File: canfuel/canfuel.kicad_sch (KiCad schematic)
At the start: 0 parts

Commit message: Draw canfuel schematic
One A3 sheet, 22 components, 31 nets. A4 was tried first and every block
collided with its neighbour - the part count is low but the label count
is not.

All four failure modes from section 3 of the implementation plan are on
the sheet and repeated as numbered notes on it, so they survive even if
someone opens the schematic without the plan: MCP2562 VIO to +5V and STBY
to SGND, R5 120R not fitted, 33 pF crystal loading, both Micro-Fit headers
in parallel, and 10 uF on VDDCORE/VCAP with pin 6 never tied to +5V.

Labels are global rather than local. On one sheet either works, but a
local label reaches the netlist as /CANH while the net classes in plan
section 5.3 are written CANH, and a netclass pattern matching nothing is
a bad way to discover that CAN got routed at the default track width.

U1 uses the SSOP-28 symbol with a PDIP-28 socket footprint - KiCad ships
no SPDIP variant for this part and all three 28-pin packages share one
pinout, verified pin by pin against DS39977C page 6.

ERC is clean at --severity-all with nothing silenced; three PWR_FLAGs
were needed because +5V and SGND come from a connector and VCAP from the
regulator inside U1. Separately, the exported netlist was compared
connection by connection against the plan's tables - 97 connections, no
pin unaccounted for. ERC cannot tell RB2 from RB3; that comparison can.

Co-Authored-By: Claude Opus 5 <noreply@anthropic.com>
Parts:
- added C1, C2: 33p, Capacitor_THT:C_Disc_D5.0mm_W2.5mm_P5.00mm, symbol Device:C
- added C3, C4, C5: 100n, Capacitor_THT:C_Disc_D5.0mm_W2.5mm_P5.00mm, symbol Device:C
- added C6: 10u, Capacitor_THT:CP_Radial_D5.0mm_P2.50mm, symbol Device:C_Polarized
- added C7: 10u, Capacitor_THT:C_Disc_D7.5mm_W5.0mm_P5.00mm, symbol Device:C
- added D1: green, LED_THT:LED_D3.0mm, symbol Device:LED
- added D2: yellow, LED_THT:LED_D3.0mm, symbol Device:LED
- added J1, J2: Micro-Fit 43045-0400, Connector_Molex:Molex_Micro-Fit_3.0_43045-0400_2x02_P3.00mm_Horizontal, symbol Connector_Generic:Conn_02x02_Odd_Even
- added J3: ICSP, Connector_PinHeader_2.54mm:PinHeader_1x05_P2.54mm_Vertical, symbol Connector_Generic:Conn_01x05
- added J4: ESCAPE, Connector_PinHeader_2.54mm:PinHeader_2x08_P2.54mm_Vertical, symbol Connector_Generic:Conn_02x08_Odd_Even
- added JP1: DBG, Connector_PinHeader_2.54mm:PinHeader_1x02_P2.54mm_Vertical, symbol Connector_Generic:Conn_01x02
- added R1, R2: 10k, Resistor_THT:R_Axial_DIN0207_L6.3mm_D2.5mm_P10.16mm_Horizontal, symbol Device:R
- added R3, R4: 1k, Resistor_THT:R_Axial_DIN0207_L6.3mm_D2.5mm_P10.16mm_Horizontal, symbol Device:R
- added R5: 120R, Resistor_THT:R_Axial_DIN0207_L6.3mm_D2.5mm_P10.16mm_Horizontal, symbol Device:R
- added U1: PIC18F25K80, Package_DIP:DIP-28_W7.62mm_Socket, symbol MCU_Microchip_PIC18:PIC18F25K80_ISS
- added U2: MCP2562-E/P, Package_DIP:DIP-8_W7.62mm_Socket, symbol Interface_CAN_LIN:MCP2562-E-P
- added Y1: 16MHz, Crystal:Crystal_HC49-U_Vertical, symbol Device:Crystal
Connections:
- new net +5V: C3.1, C4.1, C5.1, C6.1, J1.1 (Pin_1), J2.1 (Pin_1), J3.2 (Pin_2), J4.14 (Pin_14), JP1.1 (Pin_1), R1.1, U1.20 (Vdd), U2.3 (VDD), U2.5 (Vio)
- new net CANH: J1.3 (Pin_3), J2.3 (Pin_3), R5.1, U2.7 (CANH)
- new net CANL: J1.4 (Pin_4), J2.4 (Pin_4), R5.2, U2.6 (CANL)
- new net CANRX2: J4.4 (Pin_4), U1.18 (CANRX/RX1/CCP4/RC7)
- new net CANTX2: J4.2 (Pin_2), U1.17 (CANTX/TX1/CCP3/RC6)
- new net CAN_RX: U1.24 (CANRX/INT3/RB3), U2.4 (RXD)
- new net CAN_TX: U1.23 (CANTX/INT2/RB2), U2.1 (TXD)
- new net DBG_EN: JP1.2 (Pin_2), R2.1, U1.2 (RA0/AN0)
- new net ESC_RA3: J4.1 (Pin_1), U1.5 (RA3/Vref+/AN3)
- new net ESC_RA5: J4.3 (Pin_3), U1.7 (RA5/AN4)
- new net ESC_RB0: J4.6 (Pin_6), U1.21 (AN10/INT0/RB0)
- new net ESC_RB1: J4.8 (Pin_8), U1.22 (AN8/INT1/RB1)
- new net ESC_RB4: J4.10 (Pin_10), U1.25 (AN9/ECCP1/RB4)
- new net ESC_RB5: J4.12 (Pin_12), U1.26 (CCP5/RB5)
- new net ESC_RC0: J4.5 (Pin_5), U1.11 (SOSCO/RC0)
- new net ESC_RC1: J4.7 (Pin_7), U1.12 (SOSCI/RC1)
- new net ESC_RC2: J4.9 (Pin_9), U1.13 (CCP2/RC2)
- new net ESC_RC3: J4.11 (Pin_11), U1.14 (SCL/SCK/RC3)
- new net ESC_RC4: J4.13 (Pin_13), U1.15 (SDA/SDI/RC4)
- new net ESC_RC5: J4.15 (Pin_15), U1.16 (SDO/RC5)
- new net LED_CAN: R4.1, U1.4 (RA2/Vref-/AN2)
- new net LED_CAN_A: D2.2 (A), R4.2
- new net LED_PWR: R3.1, U1.3 (RA1/AN1)
- new net LED_PWR_A: D1.2 (A), R3.2
- new net OSC1: C1.1, U1.9 (OSC1/CLKIN), Y1.1
- new net OSC2: C2.1, U1.10 (OSC2/CLKOUT), Y1.2
- new net PGC: J3.5 (Pin_5), U1.27 (PGC/TX2/RB6)
- new net PGD: J3.4 (Pin_4), U1.28 (PGD/RX2/RB7)
- new net SGND: C1.2, C2.2, C3.2, C4.2, C5.2, C6.2, C7.2, D1.1 (K), D2.1 (K), J1.2 (Pin_2), J2.2 (Pin_2), J3.3 (Pin_3), J4.16 (Pin_16), R2.2, U1.19 (Vss), U1.8 (Vss), U2.2 (VSS), U2.8 (STBY)
- new net VCAP: C7.1, U1.6 (Vcap)
- new net ~{MCLR}: J3.1 (Pin_1), R1.2, U1.1 (~{MCLR}/RE3)
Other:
- note added: "5 J1 and J2 are wired in parallel on the same four nets, so the cables are interchangeable and the board passes CAN through even with U1 out of its socket. Micro-Fit pin 1 = +5V, 2 = SGND, 3 = CANH, 4 = CANL, fixed by the harness. 6 Decoupling: C3 at U1 pin 20, C4 at U2 pin 3, C5 at U2 pin 5. 7 No pull-ups, series diodes or capacitors on PGC/PGD - they interfere with the programmer. DS39977C 2.5.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"
- note added: "NOTES 1 U2 VIO (pin 5) to +5V and STBY (pin 8) to SGND are both mandatory. Left off, the transceiver sits in standby and sends nothing while every other measurement looks correct. 2 C7 is 10 uF low-ESR on VDDCORE/VCAP (U1 pin 6) and is not optional - the core regulator is unstable without it. Pin 6 is not a port pin and must NEVER go to +5V. Keep the PCB track to C7 under 6 mm. DS39977C 2.4 and t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"
- company: (none) -> PoJD
- title: (none) -> canfuel - CAN fuel consumption converter

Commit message: Re-check the schematic against the manufacturer datasheets
Adopts a sourcing rule for this repository: every hardware fact comes from the
manufacturer's datasheet for the exact part, cited by document and section, and
an open question is asked rather than filled in with a plausible number. The
rule is in CLAUDE.md; implementation-plan.md section 10 lists what has actually
been read out of each datasheet, so a checked number can be told from an
inherited one.

Applying it to the drawn sheet found three things.

The LEDs were on RA1/RA2, which are inside PORTA<5:0>. DS39977C page 541 caps
those pins at 2 mA sourced or sunk, against 25 mA for PORTB and PORTC; 1 kohm
from a 5 V rail draws about 2.2 mA once VOH is taken as VDD-0.7. They move to
RC0 (pin 11) and RC1 (pin 12) and RA1/RA2 take the escape-header slots RC0/RC1
vacate, so J4 stays 2x8 and the board is unchanged. The DC characteristics
table specifies PORTA at IOH = -3 mA and so reads like permission; absolute
maximums win. PoJD/can-pcb was not a precedent for the 1 kohm - its status LED
is on RC1, and the port was the part that mattered.

MCLR had only the 10k pull-up, with a note reading "no capacitor on this pin".
That was section 2.5, which is about PGC and PGD, applied to MCLR. Section 2.3
asks for the capacitor and hands it a jumper in the same paragraph, so the full
Figure 2-2 network goes in: R6 470R in series into pin 1, C8 100n to SGND
behind JP2. JP2 comes off before programming.

The crystal was documented as CL = 32 pF. That figure is in no datasheet and
does not survive the arithmetic - 32 pF would want about 56 pF of loading. The
supplied crystal datasheet gives 20 pF standard, and C = 2*(20-5) = 30 pF puts
the fitted 33 pF exactly where it should be. The value was right for the wrong
reason. No series resistor on OSC2: the drive level argues for one, the
datasheet only says "may be required", and it cannot be settled without
measuring a built board.

Also recorded: STBY floats high through an in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
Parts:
- added C8: 100n, Capacitor_THT:C_Disc_D5.0mm_W2.5mm_P5.00mm, symbol Device:C
- added JP2: MCLR, Connector_PinHeader_2.54mm:PinHeader_1x02_P2.54mm_Vertical, symbol Connector_Generic:Conn_01x02
- added R6: 470R, Resistor_THT:R_Axial_DIN0207_L6.3mm_D2.5mm_P10.16mm_Horizontal, symbol Device:R
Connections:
- net ESC_RA3: now also J4.5 (Pin_5); no longer J4.1 (Pin_1)
- net ESC_RA5: now also J4.7 (Pin_7); no longer J4.3 (Pin_3)
- net LED_CAN: now also U1.12 (SOSCI/RC1); no longer U1.4 (RA2/Vref-/AN2)
- net LED_PWR: now also U1.11 (SOSCO/RC0); no longer U1.3 (RA1/AN1)
- net SGND: now also C8.2
- net ~{MCLR}: now also R6.2; no longer R1.2
- removed net ESC_RC0: J4.5 (Pin_5), U1.11 (SOSCO/RC0)
- removed net ESC_RC1: J4.7 (Pin_7), U1.12 (SOSCI/RC1)
- new net ESC_RA1: J4.1 (Pin_1), U1.3 (RA1/AN1)
- new net ESC_RA2: J4.3 (Pin_3), U1.4 (RA2/Vref-/AN2)
- new net MCLR_C: C8.1, JP2.2 (Pin_2)
- new net MCLR_RC: JP2.1 (Pin_1), R1.2, R6.1
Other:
- note added: "10 D1 and D2 sit on RC0 and RC1, not on port A. DS39977C page 541 allows PORTA<5:0> only 2 mA sourced or sunk, against 25 mA on PORTB and PORTC. RA1 and RA2 went to J4 instead. 11 MCLR carries the full network of DS39977C figure 2-2: R1 10k to +5V, R6 470R in series into pin 1, C8 100n to SGND behind JP2. Pull the JP2 jumper before programming - note 7."

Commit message: Pin C6 and C7 to the parts that will actually be fitted
Both capacitors carried a footprint that no purchasable part matched, which
would have surfaced during layout at the earliest and during assembly at the
worst.

C6 was drawn on a 2.50 mm radial pattern. The electrolytic bought for it is a
5 x 11 mm RM2 part, so the footprint becomes CP_Radial_D5.0mm_P2.00mm.

C7 was drawn as a 5 mm ceramic disc, and no such 10 uF part exists to buy -
GME's through-hole ceramic range stops at 1 uF. It becomes a Murata
GRM32DR71C106KA01L in 1210, which is one of the four parts DS39977C Table 2-1
names for this pin, so its suitability needs no equivalence argument: ESR in
milliohms against a 5 ohm limit, and enough DC-bias headroom in a 1210 X7R at
3.3 V to stay clear of the 4.7 uF minimum in Table 31-4.

A dipped tantalum was the obvious way to keep the board entirely through-hole
and was rejected on the evidence. The CA42 datasheet gives DF = 6 % at 100 Hz
across the 10-68 uF range, which is 9.6 ohm there, and specifies no
high-frequency ESR at all. The true figure is probably 2-3 ohm and PoJD/can-pcb
has run one for years, but that is experience rather than specification, and
this is the part whose failure mode section 3.5 already describes as
intermittent and unpleasant to debug. Recorded in the plan so the option is not
reopened from memory. A tantalum would also have needed C_Polarized and a
polarity mark; can-pcb drew its as a non-polarised C-EU, which was safe only
because the builder knew which way round it went.

C7 is now the only SMD part on the board. That buys something back: at 1210 it
goes on B.Cu directly under pin 6, which turns the 6 mm track limit of section
2.4 - the one numeric placement constraint on this board - into roughly zero.

Also relaxes the buying rule for resistors and LEDs, which was inherited
without a reason. Neither has an electrolyte or a hidden parameter, so neither
ages in a drawer; the rule was only ever about the electrolytic and about a
c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
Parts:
- C6: footprint Capacitor_THT:CP_Radial_D5.0mm_P2.50mm -> Capacitor_THT:CP_Radial_D5.0mm_P2.00mm
- C7: footprint Capacitor_THT:C_Disc_D7.5mm_W5.0mm_P5.00mm -> Capacitor_SMD:C_1210_3225Metric_Pad1.33x2.70mm_HandSolder
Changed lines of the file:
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@@
 		(property
 			"Footprint"
-			"Capacitor_THT:C_Disc_D7.5mm_W5.0mm_P5.00mm"
+			"Capacitor_SMD:C_1210_3225Metric_Pad1.33x2.70mm_HandSolder"
 			(at 99.06 76.2 0)
 			(show_name no)
@@
 		(property
 			"Footprint"
-			"Capacitor_THT:CP_Radial_D5.0mm_P2.50mm"
+			"Capacitor_THT:CP_Radial_D5.0mm_P2.00mm"
 			(at 91.44 215.9 0)
 			(show_name no)

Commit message: Place canfuel PCB parts
Net classes, all 25 footprints, and a silkscreen that can be read. Nothing is
routed yet; DRC is clean and the 70 unconnected items are the ratsnest.

The MCLR network cannot meet DS39977C 2.3 in full. Four parts totalling 71 mm2
of courtyard do not fit in the ~85 mm2 of free area around a corner pin of a
DIP-28, whatever footprints are chosen. R6, the series resistor in the reset
path, is inside the 6 mm circle entirely; C8 and JP2 sit 4.31 and 2.04 mm away
at their near edges; R1, the static pull-up, is the one pushed out. Those
figures are recorded in ALLOW in tools/check-placement.py with their reasons.

R1-R6 became upright P2.54mm parts and C8 a 2.50 mm disc. That is how the
maintainer fits axial resistors anyway, and it is the only reason R6 fits at
all: 3.95 mm reach standing against 11.36 mm lying down.

C7 is turned across U1 rather than along it. Lying along the pin row its ground
pad shorted pin 5; in the channel between the rows it clears both by 0.79 mm
and still lands 2.25 mm from pin 6.

Two new tools, because neither DRC nor kicad-cli covers this ground:

  check-placement.py   measures the four datasheet distance rules and the
                       mounting-hole keepouts. DRC will happily pass a board
                       with a decoupling capacitor 40 mm from its pin.
  import-footprints.py Update PCB from Schematic without the GUI; kicad-cli
                       has no equivalent. Safe to re-run - placement survives.

Also corrects the CLAUDE.md note claiming permissions use defaultMode dontAsk.
They do not, and should not: dontAsk does not widen the allow list, so unmatched
commands are silently rejected instead of prompting.

Co-Authored-By: Claude Opus 5 <noreply@anthropic.com>
Claude-Session: https://claude.ai/code/session_01UuRx2iytAQXHULyNP41hBq
@
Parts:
- C8: footprint Capacitor_THT:C_Disc_D5.0mm_W2.5mm_P5.00mm -> Capacitor_THT:C_Disc_D5.0mm_W2.5mm_P2.50mm
- R1, R2, R3, R4, R5, R6: footprint Resistor_THT:R_Axial_DIN0207_L6.3mm_D2.5mm_P10.16mm_Horizontal -> Resistor_THT:R_Axial_DIN0207_L6.3mm_D2.5mm_P2.54mm_Vertical
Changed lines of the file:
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@@
 		(property
 			"Footprint"
-			"Resistor_THT:R_Axial_DIN0207_L6.3mm_D2.5mm_P10.16mm_Horizontal"
+			"Resistor_THT:R_Axial_DIN0207_L6.3mm_D2.5mm_P2.54mm_Vertical"
 			(at 127 127 0)
 			(show_name no)
@@
 		(property
 			"Footprint"
-			"Resistor_THT:R_Axial_DIN0207_L6.3mm_D2.5mm_P10.16mm_Horizontal"
+			"Resistor_THT:R_Axial_DIN0207_L6.3mm_D2.5mm_P2.54mm_Vertical"
 			(at 160.02 152.4 0)
 			(show_name no)
@@
 		(property
 			"Footprint"
-			"Resistor_THT:R_Axial_DIN0207_L6.3mm_D2.5mm_P10.16mm_Horizontal"
+			"Resistor_THT:R_Axial_DIN0207_L6.3mm_D2.5mm_P2.54mm_Vertical"
 			(at 261.62 203.2 0)
 			(show_name no)
@@
 		(property
 			"Footprint"
-			"Resistor_THT:R_Axial_DIN0207_L6.3mm_D2.5mm_P10.16mm_Horizontal"
+			"Resistor_THT:R_Axial_DIN0207_L6.3mm_D2.5mm_P2.54mm_Vertical"
 			(at 302.26 203.2 0)
 			(show_name no)
@@
 		(property
 			"Footprint"
-			"Resistor_THT:R_Axial_DIN0207_L6.3mm_D2.5mm_P10.16mm_Horizontal"
+			"Resistor_THT:R_Axial_DIN0207_L6.3mm_D2.5mm_P2.54mm_Vertical"
 			(at 342.9 127 0)
 			(show_name no)
@@
 		(property
 			"Footprint"
-			"Resistor_THT:R_Axial_DIN0207_L6.3mm_D2.5mm_P10.16mm_Horizontal"
+			"Resistor_THT:R_Axial_DIN0207_L6.3mm_D2.5mm_P2.54mm_Vertical"
 			(at 127 172.72 0)
 			(show_name no)
@@
 		(property
 			"Footprint"
-			"Capacitor_THT:C_Disc_D5.0mm_W2.5mm_P5.00mm"
+			"Capacitor_THT:C_Disc_D5.0mm_W2.5mm_P2.50mm"
 			(at 172.72 172.72 0)
 			(show_name no)

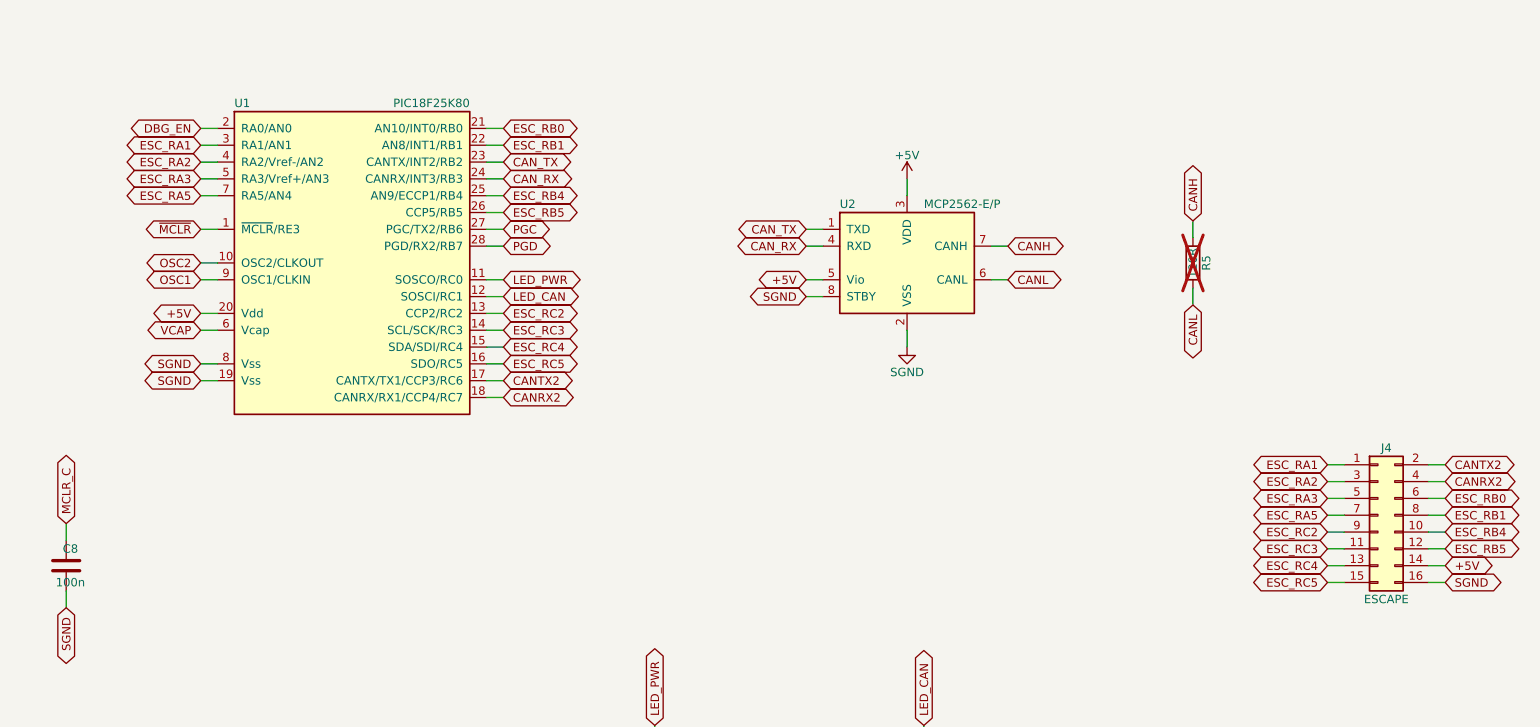
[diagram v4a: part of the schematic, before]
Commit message: Route canfuel PCB, and drop the escape header
DRC is clean with zero unconnected items. Two layers, SGND poured on both,
thermal reliefs on every pad because the board is hand soldered.

J4 is gone, and it went on measurement rather than argument. Routing the same
placement with the same router, with and without it:

                        with J4   without J4
  connections               39           25
  left unroutable            8            0
  DRC                incomplete   0 violations

Five of those eight failures were not escape signals: both status LEDs and the
whole ICSP header. J4's fourteen signals congest the channel between U1's pin
rows, which is the only way across a 55 x 45 mm board, and ICSP is what
starves. A header that exists to rescue a design error was stopping the chip
being programmed. Patching now goes onto the PDIP socket pins from underneath,
which was always the real escape hatch.

U1's fourteen unused pins carry no-connect flags. check-netlist.py grew an NC
sentinel for them rather than transcribing the generated net names.

The freed column turned out to sit inside the 6 mm circle DS39977C 2.3 draws
around pin 1, which is why the MCLR cluster could never be tightened before.
Re-placed by search: worst far corner 10.68 -> 8.67 mm, and all four parts now
within 2.5 mm of the pin at their nearest edge. The earlier arrangement had R6
wholly inside but left C8 - the reset capacitor, the part the section's own
Figure 2-2 note is about - furthest away.

check-placement.py now also asserts what 2.6 says about copper: no signal or
power traces inside the oscillator guard, nothing at all on B.Cu under the
crystal. Both are given to the router as keep-outs and re-checked afterwards,
so they cannot quietly rot.

Two things the routing taught, recorded in plan 5.3:

  Net order decides whether it finishes. Oscillator and VCAP first then the
  rest alphabetically managed 32 of 39; longest-first managed 25 and +5V-last
  managed 27. The 0.8 mm +5V 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
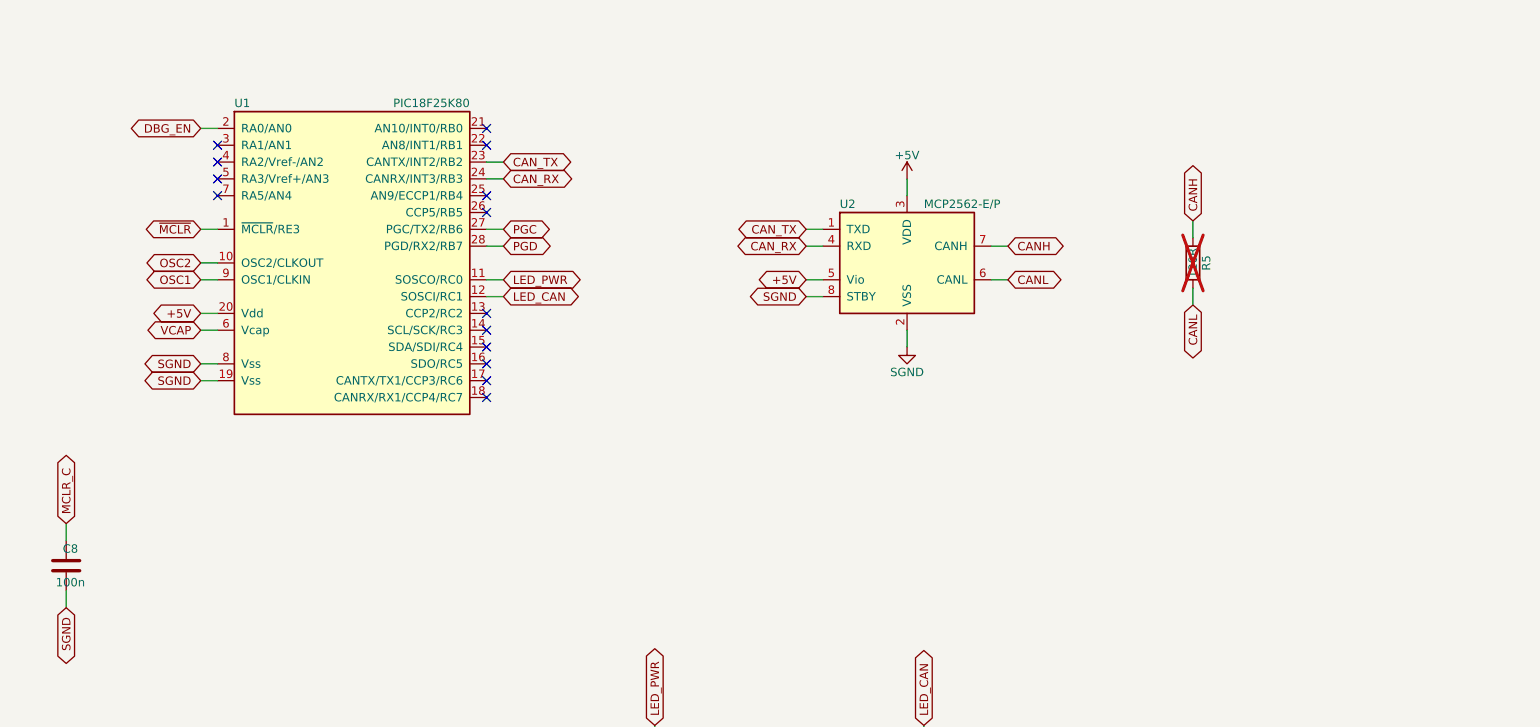
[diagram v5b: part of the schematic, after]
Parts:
- removed J4: ESCAPE, Connector_PinHeader_2.54mm:PinHeader_2x08_P2.54mm_Vertical, symbol Connector_Generic:Conn_02x08_Odd_Even
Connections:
- net CANRX2: no longer names the net of U1.18 (CANRX/RX1/CCP4/RC7)
- net CANTX2: no longer names the net of U1.17 (CANTX/TX1/CCP3/RC6)
- net ESC_RA1: no longer names the net of U1.3 (RA1/AN1)
- net ESC_RA2: no longer names the net of U1.4 (RA2/Vref-/AN2)
- net ESC_RA3: no longer names the net of U1.5 (RA3/Vref+/AN3)
- net ESC_RA5: no longer names the net of U1.7 (RA5/AN4)
- net ESC_RB0: no longer names the net of U1.21 (AN10/INT0/RB0)
- net ESC_RB1: no longer names the net of U1.22 (AN8/INT1/RB1)
- net ESC_RB4: no longer names the net of U1.25 (AN9/ECCP1/RB4)
- net ESC_RB5: no longer names the net of U1.26 (CCP5/RB5)
- net ESC_RC2: no longer names the net of U1.13 (CCP2/RC2)
- net ESC_RC3: no longer names the net of U1.14 (SCL/SCK/RC3)
- net ESC_RC4: no longer names the net of U1.15 (SDA/SDI/RC4)
- net ESC_RC5: no longer names the net of U1.16 (SDO/RC5)
- no-connect marks 0 -> 14
